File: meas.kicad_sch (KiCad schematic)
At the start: 0 parts

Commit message: add digital-interface schematic
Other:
- added sheet digital-interface (digital-interface.kicad_sch)
- added sheet digital-interface1 (digital-interface.kicad_sch)
- added sheet digital-interface2 (digital-interface.kicad_sch)
- added sheet digital-interface3 (digital-interface.kicad_sch)

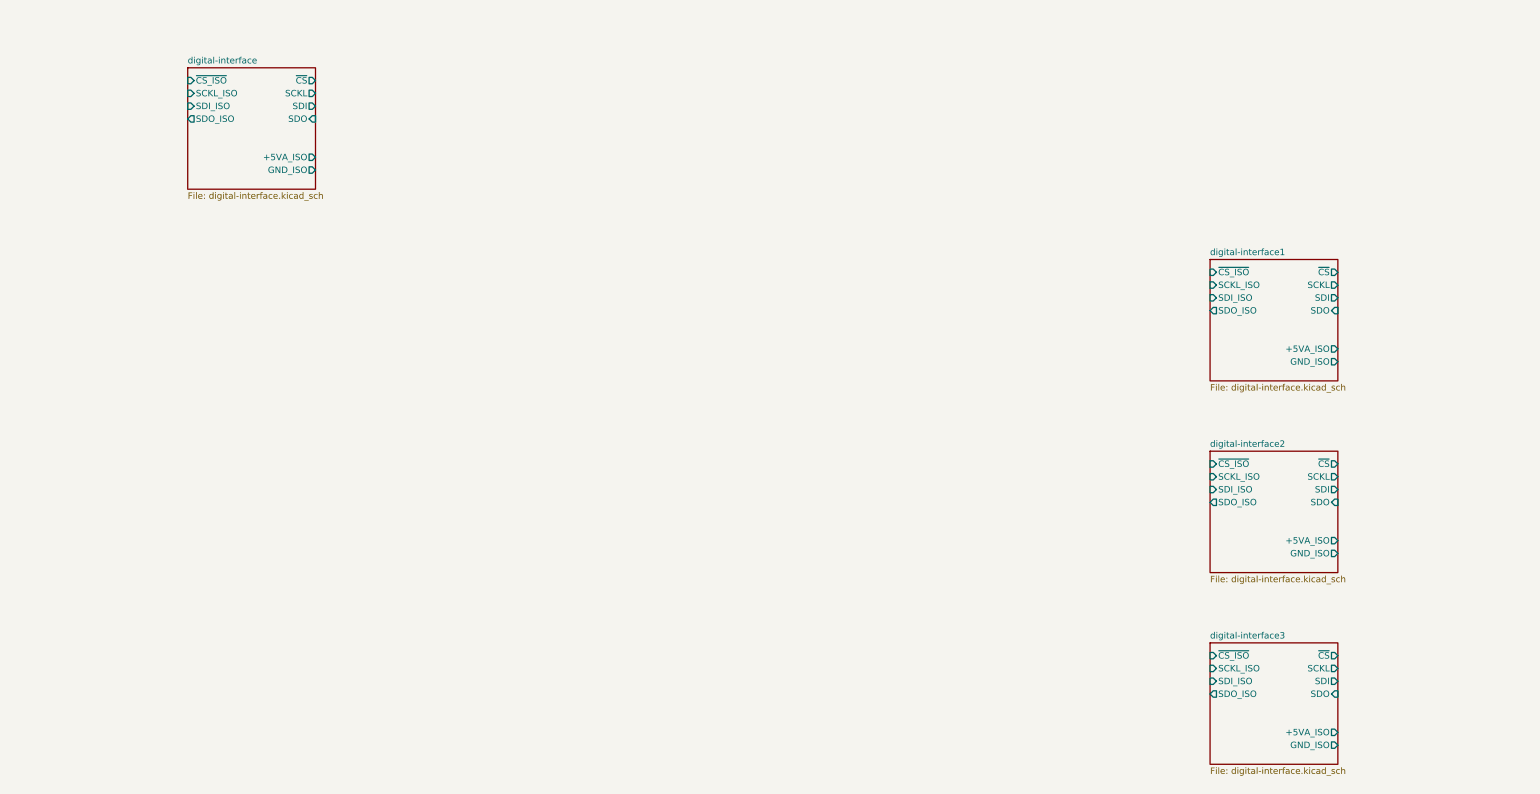
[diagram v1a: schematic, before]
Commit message: add adc schematic
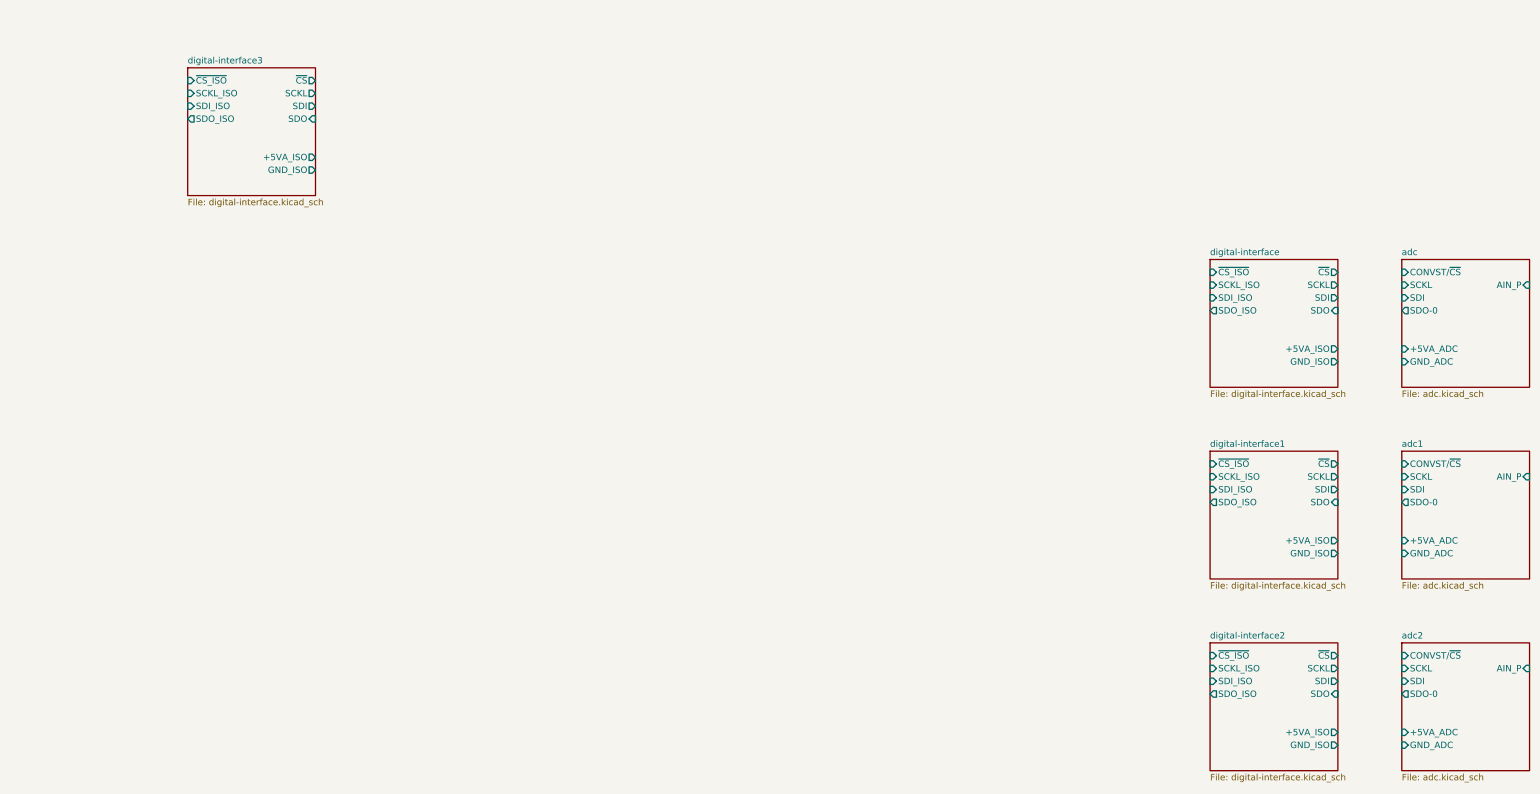
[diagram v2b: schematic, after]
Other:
- added sheet adc (adc.kicad_sch)
- added sheet adc1 (adc.kicad_sch)
- added sheet adc2 (adc.kicad_sch)

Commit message: add i-transduce schematic
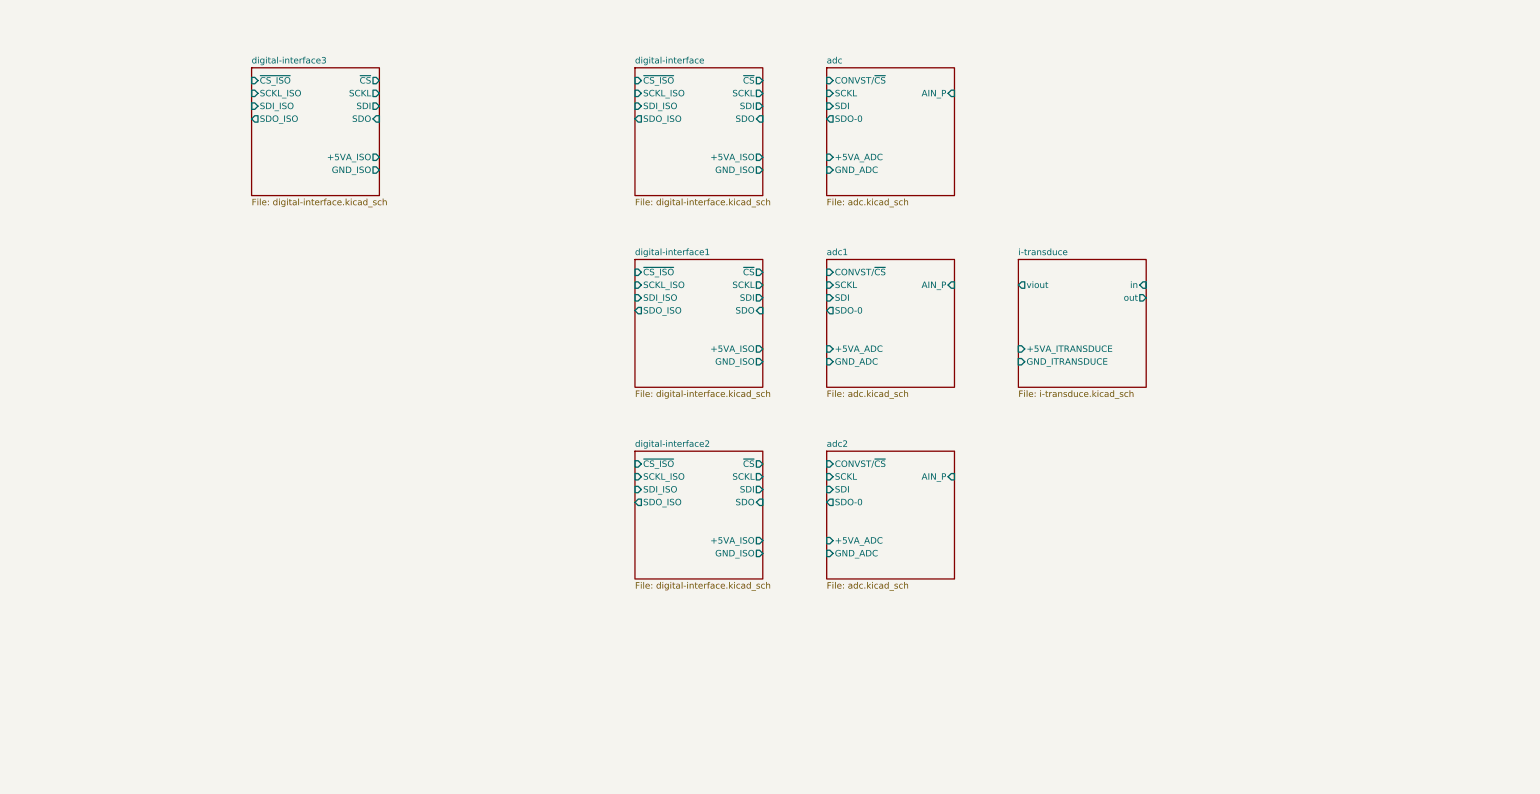
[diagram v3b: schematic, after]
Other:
- added sheet i-transduce (i-transduce.kicad_sch)

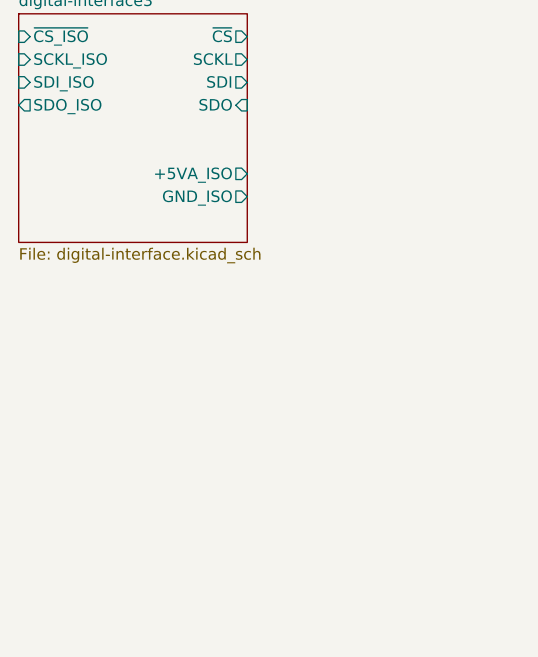
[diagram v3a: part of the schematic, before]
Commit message: add power schematic
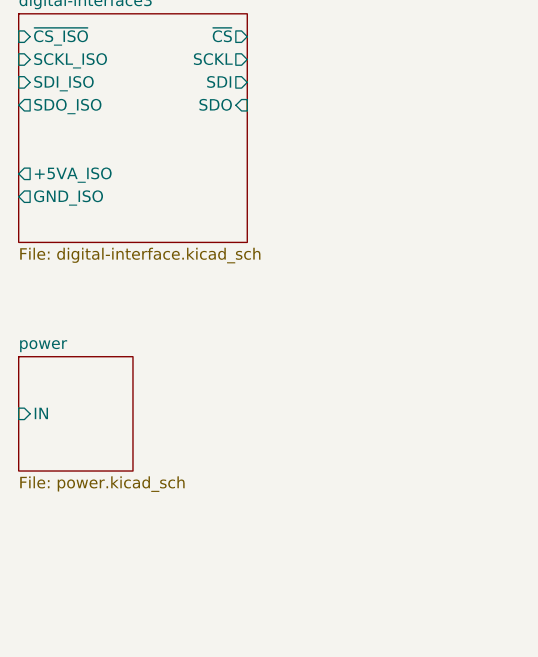
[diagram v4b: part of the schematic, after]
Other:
- added sheet power (power.kicad_sch)
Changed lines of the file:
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@@
+	)
+	(sheet
+		(at 63.5 76.2)
+		(size 12.7 12.7)
+		(fields_autoplaced yes)
+		(stroke
+			(width 0.1524)
+			(type solid)
+		)
+		(fill
+			(color 0 0 0 0.0000)
+		)
+		(property "Sheetname" "power"
+			(at 63.5 75.4884 0)
+			(effects
+				(font
+					(size 1.27 1.27)
+				)
+				(justify left bottom)
+			)
+		)
+		(property "Sheetfile" "power.kicad_sch"
+			(at 63.5 89.4846 0)
+			(effects
+				(font
+					(size 1.27 1.27)
+				)
+				(justify left top)
+			)
+		)
+		(pin "IN" input
+			(at 63.5 82.55 180)
+			(effects
+				(font
+					(size 1.27 1.27)
+				)
+				(justify left)
+			)
+		)
+		(instances
+			(project "meas"
+				(path "/f710e4da-f895-4fe1-9122-3234febe82c7"
+					(page "10")
+				)
+			)
+		)
 	)
 	(sheet
@@
 		)
 		(pin "GND_ISO" output
-			(at 88.9 58.42 0)
+			(at 63.5 58.42 180)
 			(effects
 				(font
 					(size 1.27 1.27)
 				)
-				(justify right)
+				(justify left)
 			)
 		)
 		(pin "+5VA_ISO" output
-			(at 88.9 55.88 0)
+			(at 63.5 55.88 180)
 			(effects
 				(font
 					(size 1.27 1.27)
 				)
-				(justify right)
+				(justify left)
 			)
 		)

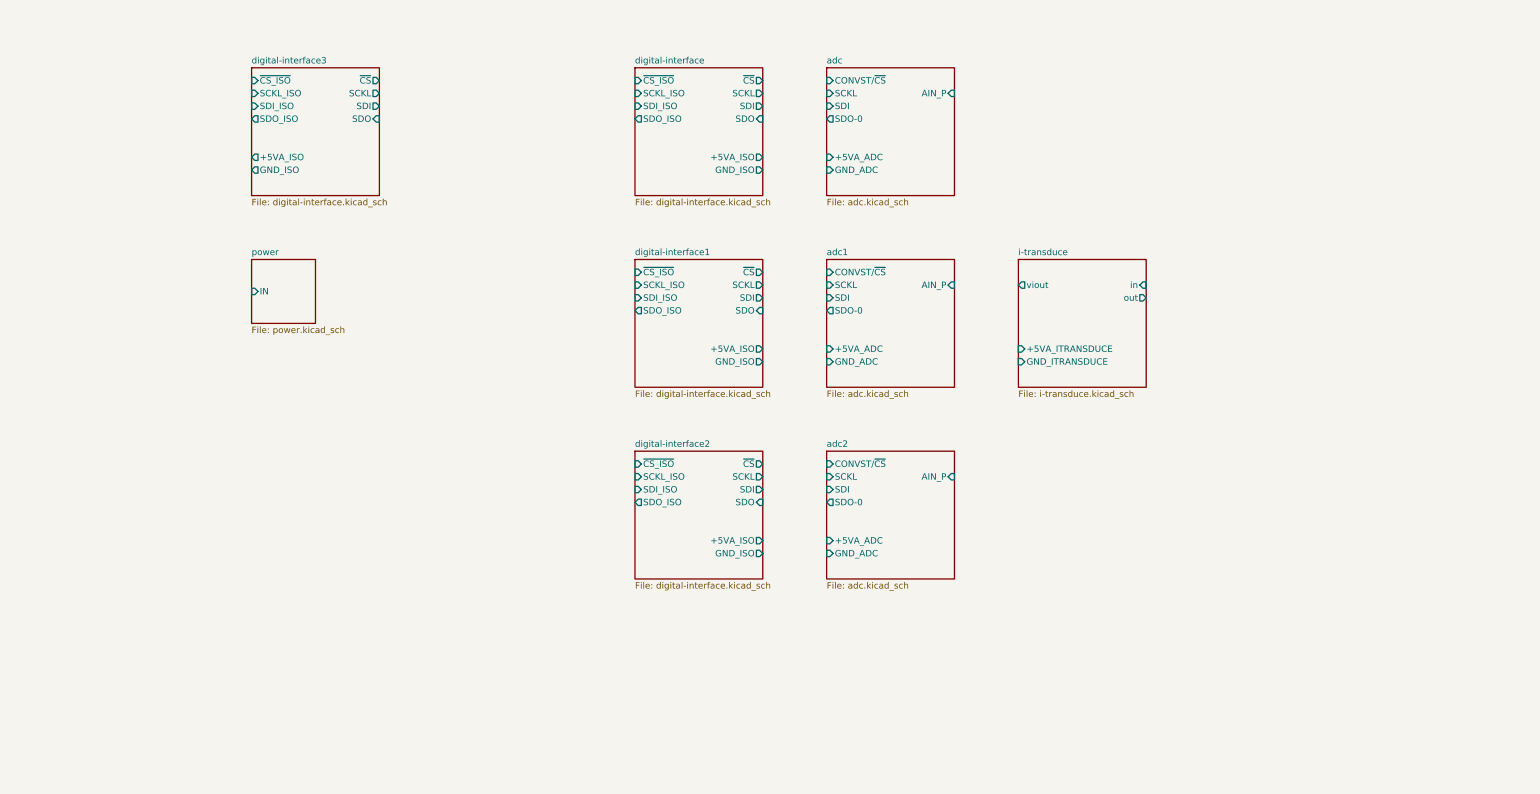
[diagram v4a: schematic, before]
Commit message: add overview schematic wiring
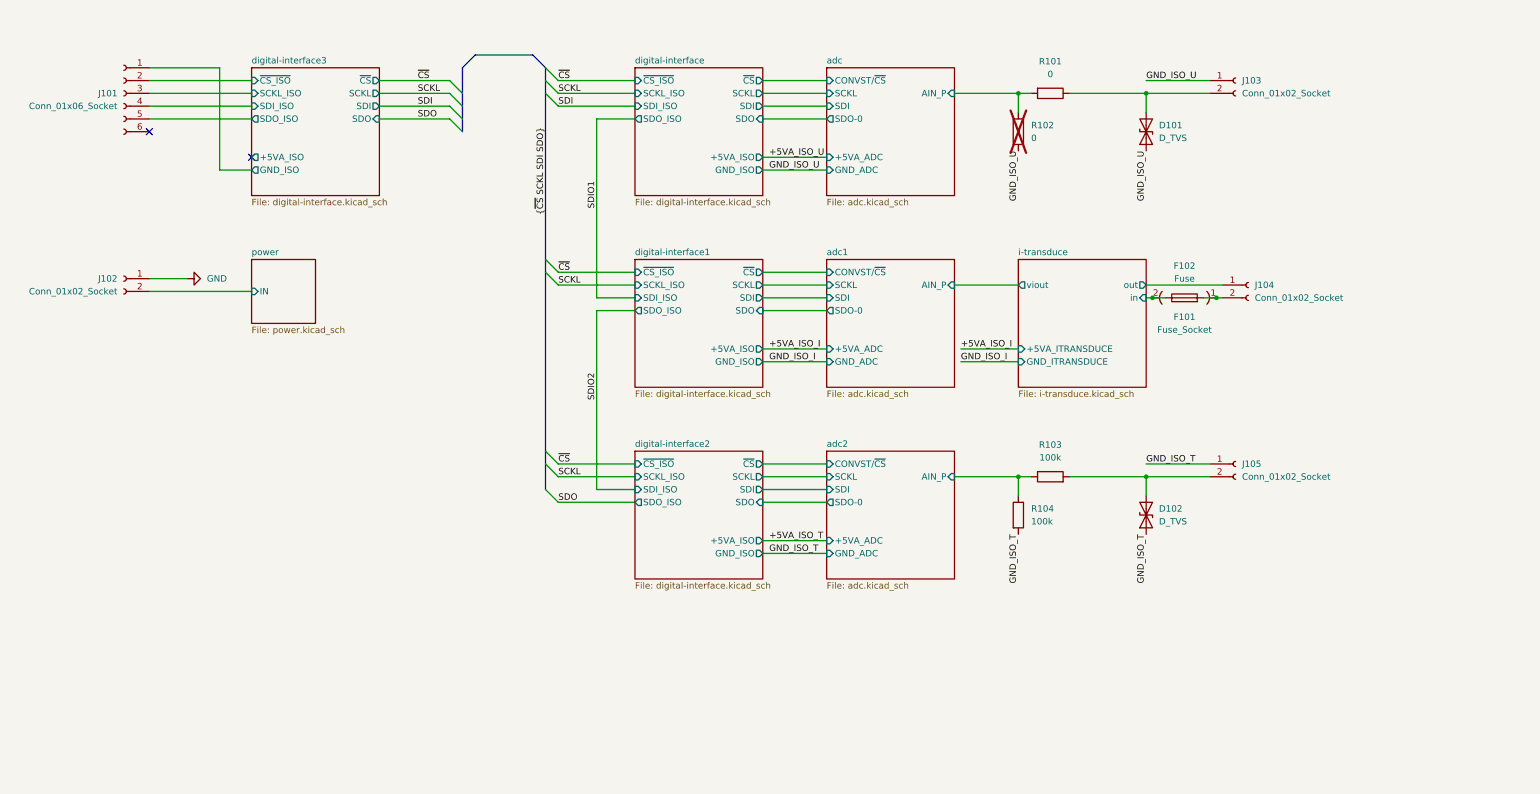
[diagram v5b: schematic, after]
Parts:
- added D101, D102: D_TVS, enclosure:D_SOD-323_HandSoldering, symbol enclosure:D_TVS
- added F101: Fuse_Socket, enclosure:FuseHolder_Blade_ATO_Littelfuse_FLR_178.6165, symbol enclosure:Fuse_Socket_1
- added F102: Fuse, symbol enclosure:Fuse
- added J101: Conn_01x06_Socket, pss:PhoenixContact_TDPT_2,5_6-SP-5,08_1x06_P5.08mm_Horizontal, symbol pss:Conn_01x06_Socket
- added J102, J103, J104, J105: Conn_01x02_Socket, pss:PhoenixContact_TDPT_2,5_2-SP-5,08_1x02_P5.08mm_Horizontal, symbol pss:Conn_01x02_Socket
- added R101, R102: 0, pss:R_1210_3225Metric_Pad1.30x2.65mm_HandSolder, symbol pss:R
- added R103, R104: 100k, pss:R_1210_3225Metric_Pad1.30x2.65mm_HandSolder, symbol pss:R
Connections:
- net adc/AIN_P: now also R101.2, R102.2
- net adc2/AIN_P: now also R103.1, R104.1
- net digital-interface3/GND_ISO: now also J101.1 (Pin_1)
- net digital-interface3/SCKL_ISO: now also J101.3 (Pin_3)
- net digital-interface3/SDI_ISO: now also J101.4 (Pin_4)
- net digital-interface3/SDO_ISO: now also J101.5 (Pin_5)
- net digital-interface3/~{CS_ISO}: now also J101.2 (Pin_2)
- net i-transduce/in: now also F101.2, F102.1
- net i-transduce/out: now also J104.1 (Pin_1)
- net power/IN: now also J102.2 (Pin_2)
- new net: D101.2 (A2), J103.2 (Pin_2), R101.1
- new net: F101.1, F102.2, J104.2 (Pin_2)
- new net: D102.2 (A2), J105.2 (Pin_2), R103.2
- new net GND: J102.1 (Pin_1)
- new net GND_ISO_T: D102.1 (A1), J105.1 (Pin_1), R104.2
- new net GND_ISO_U: D101.1 (A1), J103.1 (Pin_1), R102.1
- no-connect marks 0 -> 2

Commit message: fix digital-interface schematic connections
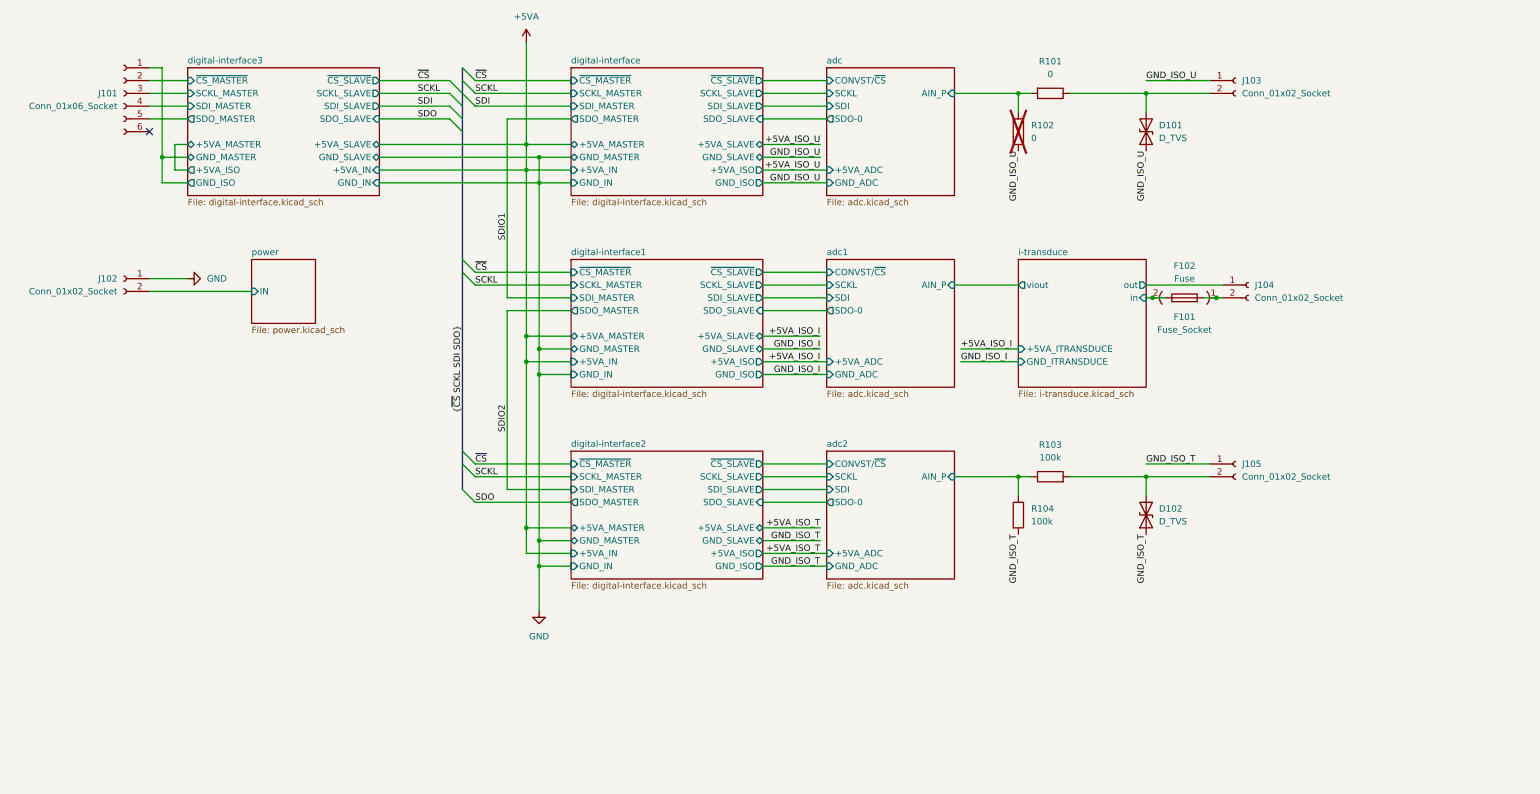
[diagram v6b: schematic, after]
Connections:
- net digital-interface3/SCKL_ISO renamed digital-interface3/SCKL_MASTER
- net digital-interface3/SDI_ISO renamed digital-interface3/SDI_MASTER
- net digital-interface3/SDO_ISO renamed digital-interface3/SDO_MASTER
- net digital-interface3/~{CS_ISO} renamed digital-interface3/~{CS_MASTER}
- no-connect marks 2 -> 1
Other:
- sheet digital-interface ports: added +5VA_IN, +5VA_MASTER, +5VA_SLAVE, GND_IN, GND_MASTER, GND_SLAVE, SCKL_MASTER, SCKL_SLAVE, SDI_MASTER, SDI_SLAVE, SDO_MASTER, SDO_SLAVE, ~{CS_MASTER}, ~{CS_SLAVE}; removed SCKL, SCKL_ISO, SDI, SDI_ISO, SDO, SDO_ISO, ~{CS_ISO}, ~{CS}
- sheet digital-interface1 ports: added +5VA_IN, +5VA_MASTER, +5VA_SLAVE, GND_IN, GND_MASTER, GND_SLAVE, SCKL_MASTER, SCKL_SLAVE, SDI_MASTER, SDI_SLAVE, SDO_MASTER, SDO_SLAVE, ~{CS_MASTER}, ~{CS_SLAVE}; removed SCKL, SCKL_ISO, SDI, SDI_ISO, SDO, SDO_ISO, ~{CS_ISO}, ~{CS}
- sheet digital-interface2 ports: added +5VA_IN, +5VA_MASTER, +5VA_SLAVE, GND_IN, GND_MASTER, GND_SLAVE, SCKL_MASTER, SCKL_SLAVE, SDI_MASTER, SDI_SLAVE, SDO_MASTER, SDO_SLAVE, ~{CS_MASTER}, ~{CS_SLAVE}; removed SCKL, SCKL_ISO, SDI, SDI_ISO, SDO, SDO_ISO, ~{CS_ISO}, ~{CS}
- sheet digital-interface3 ports: added +5VA_IN, +5VA_MASTER, +5VA_SLAVE, GND_IN, GND_MASTER, GND_SLAVE, SCKL_MASTER, SCKL_SLAVE, SDI_MASTER, SDI_SLAVE, SDO_MASTER, SDO_SLAVE, ~{CS_MASTER}, ~{CS_SLAVE}; removed SCKL, SCKL_ISO, SDI, SDI_ISO, SDO, SDO_ISO, ~{CS_ISO}, ~{CS}
